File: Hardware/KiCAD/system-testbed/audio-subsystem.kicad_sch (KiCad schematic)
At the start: 15 parts, among them U2 MAX98357A

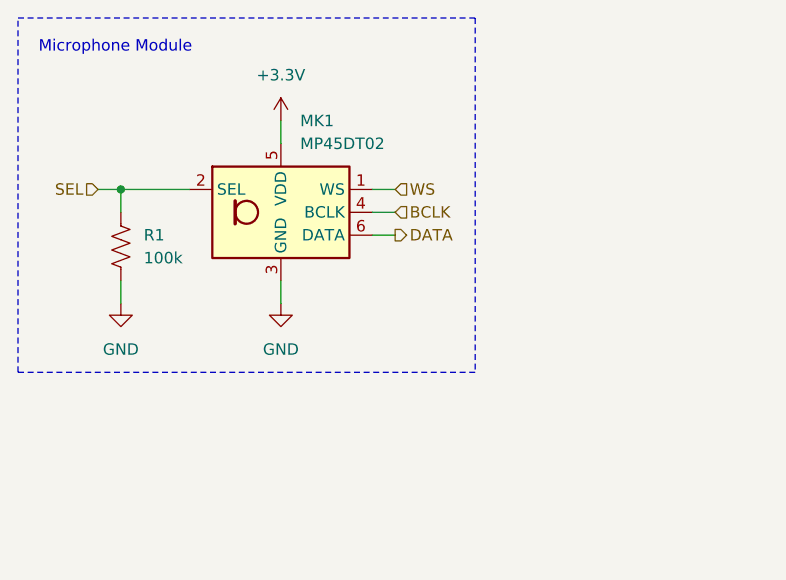
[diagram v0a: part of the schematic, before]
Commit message: fix: phase out obselete microphone module
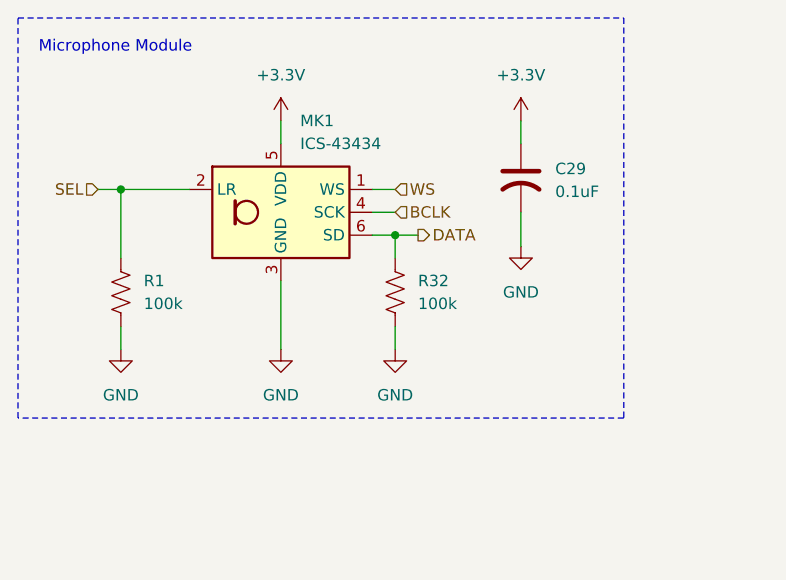
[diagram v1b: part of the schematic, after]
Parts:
- added C29: 0.1uF, symbol Device:C_US
- added R32: 100k, symbol Device:R_US
- MK1: value MP45DT02 -> ICS-43434; footprint Sensor_Audio:Knowles_SPH0645LM4H-6_3.5x2.65mm -> Sensor_Audio:InvenSense_ICS-43434-6_3.5x2.65mm; symbol Sensor_Audio:SPH0645LM4H -> Sensor_Audio:ICS-43434
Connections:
- net +3.3V: now also C29.1
- net DATA: now also R32.1
- net GND: now also C29.2, R32.2
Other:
- moved on the sheet: R1

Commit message: feat: complete recapture of Adafruit Mic Module
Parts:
- added C30: 0.1uF, symbol Device:C_US
- added R33: 68, symbol Device:R_US
- C29: value 0.1uF -> 1uF
- R1, R32: value 100k -> 47k
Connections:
- net +3.3V: now also C30.1
- net DATA: now also R33.2; no longer MK1.6 (SD), R32.1
- net GND: now also C30.2
- new net: MK1.6 (SD), R32.1, R33.1
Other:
- moved on the sheet: C29

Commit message: feat: assign 0603 passive component footprints #32 #34
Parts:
- C29, C30: footprint (none) -> Capacitor_SMD:C_0603_1608Metric
- R1, R32, R33: footprint (none) -> Resistor_SMD:R_0603_1608Metric
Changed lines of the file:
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@@
 			)
 		)
-		(property "Footprint" ""
+		(property "Footprint" "Capacitor_SMD:C_0603_1608Metric"
 			(at 86.36 38.1 0)
 			(effects
@@
 			)
 		)
-		(property "Footprint" ""
+		(property "Footprint" "Capacitor_SMD:C_0603_1608Metric"
 			(at 99.06 38.1 0)
 			(effects
@@
 			)
 		)
-		(property "Footprint" ""
+		(property "Footprint" "Resistor_SMD:R_0603_1608Metric"
 			(at 67.564 37.084 90)
 			(effects
@@
 			)
 		)
-		(property "Footprint" ""
+		(property "Footprint" "Resistor_SMD:R_0603_1608Metric"
 			(at 56.896 44.704 90)
 			(effects
@@
 			)
 		)
-		(property "Footprint" ""
+		(property "Footprint" "Resistor_SMD:R_0603_1608Metric"
 			(at 26.416 44.704 90)
 			(effects
